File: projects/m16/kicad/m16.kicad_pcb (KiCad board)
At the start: 2 copper layers, 50 x 50 mm, 53 parts, among them P1 ENC1, P2 ENC2, P3 USB_OTG, P4 Molex 475710001, P5 PWR, P7 ESP8266, P8 WS2812, SW1 RST, SW2 HWB, U1 74LS125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

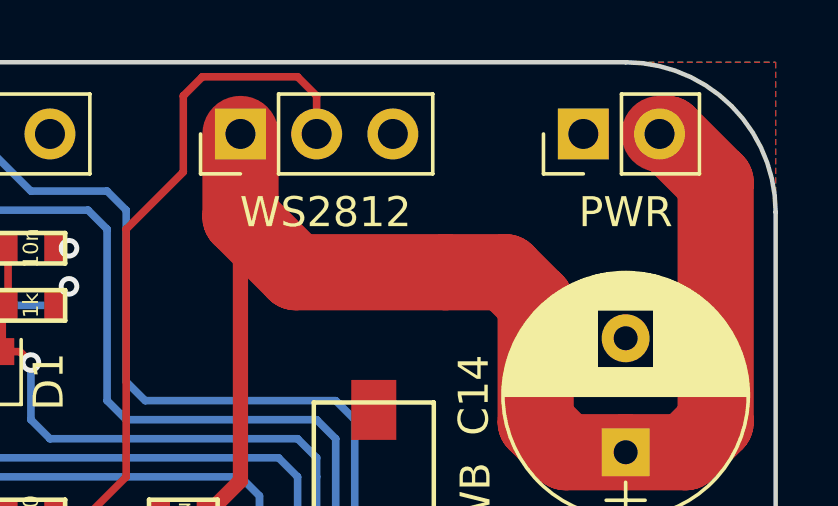
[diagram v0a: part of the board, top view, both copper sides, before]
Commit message: more copper for +5 to ws2812
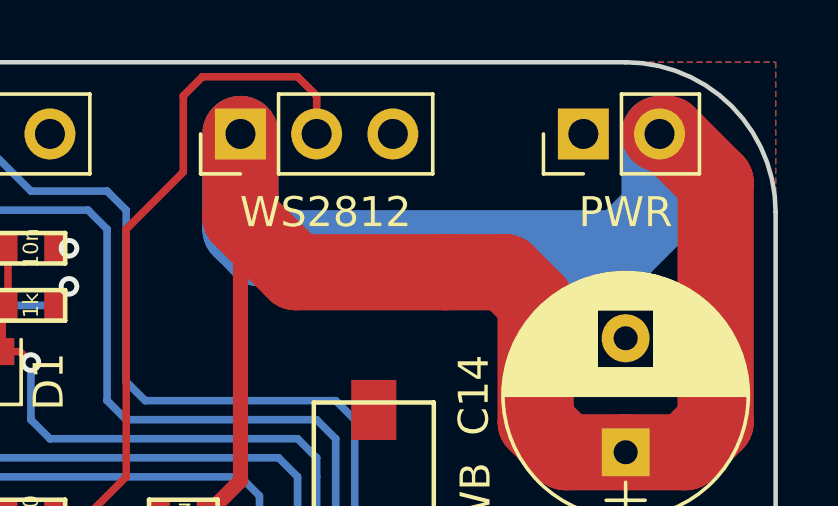
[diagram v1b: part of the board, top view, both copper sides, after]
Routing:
- net +5V: track 183.4 -> 203.9 mm
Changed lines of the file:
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@@
     (thickness 1.6)
     (drawings 14)
-    (tracks 609)
+    (tracks 614)
     (zones 0)
     (modules 53)
@@
     (35 F.Paste user)
     (36 B.SilkS user)
-    (37 F.SilkS user)
+    (37 F.SilkS user hide)
     (38 B.Mask user)
     (39 F.Mask user)
@@
   )
   (setup
-    (last_trace_width 0.254)
+    (last_trace_width 2.54)
     (user_trace_width 0.254)
     (user_trace_width 0.508)
@@
     (mod_text_size 1 1)
     (mod_text_width 0.15)
-    (pad_size 1.7 1.7)
-    (pad_drill 1)
+    (pad_size 1.6 1.6)
+    (pad_drill 0.8)
     (pad_to_mask_clearance 0.2)
     (aux_axis_origin 0 0)
@@
       (net 3 +5V) (zone_connect 2))
     (pad 2 thru_hole circle (at 3.8 0 90) (size 1.6 1.6) (drill 0.8) (layers *.Cu *.Mask)
-      (net 1 GND))
+      (net 1 GND) (zone_connect 2))
     (model ${KISYS3DMOD}/Capacitors_THT.3dshapes/CP_Radial_D8.0mm_P3.80mm.wrl
       (at (xyz 0 0 0))
@@
   (segment (start 143.05 108.95) (end 144 108) (width 0.508) (layer F.Cu) (net 2))
   (segment (start 143 113.95) (end 143.05 114) (width 0.508) (layer F.Cu) (net 2))
+  (segment (start 151.13 72.39) (end 151.13 74.93) (width 2.54) (layer B.Cu) (net 3))
+  (segment (start 137.16 75.565) (end 137.16 72.39) (width 2.54) (layer B.Cu) (net 3))
+  (segment (start 137.795 76.2) (end 137.16 75.565) (width 2.54) (layer B.Cu) (net 3))
+  (segment (start 149.86 76.2) (end 137.795 76.2) (width 2.54) (layer B.Cu) (net 3))
+  (segment (start 151.13 74.93) (end 149.86 76.2) (width 2.54) (layer B.Cu) (net 3))
   (segment (start 124.46 102.997) (end 123.063 102.997) (width 0.508) (layer F.Cu) (net 3))
   (segment (start 122.428 103.632) (end 122.428 104.775) (width 0.508) (layer F.Cu) (net 3))
@@
   (segment (start 135.715 85.2) (end 135.715 85.5) (width 0.508) (layer F.Cu) (net 3))
   (segment (start 150 83) (end 148 83) (width 2.54) (layer F.Cu) (net 3))
+  (segment (start 148 83) (end 147 82) (width 2.54) (layer F.Cu) (net 3))
+  (segment (start 147 82) (end 147 78) (width 2.54) (layer F.Cu) (net 3))
+  (segment (start 147 78) (end 146 77) (width 2.54) (layer F.Cu) (net 3))
+  (segment (start 146 77) (end 144 77) (width 2.54) (layer F.Cu) (net 3))
+  (segment (start 137.16 75.16) (end 137.16 72.39) (width 2.54) (layer F.Cu) (net 3))
+  (segment (start 139 77) (end 144 77) (width 2.54) (layer F.Cu) (net 3))
   (segment (start 137.16 75.16) (end 139 77) (width 2.54) (layer F.Cu) (net 3))
-  (segment (start 139 77) (end 144 77) (width 2.54) (layer F.Cu) (net 3))
-  (segment (start 137.16 75.16) (end 137.16 72.39) (width 2.54) (layer F.Cu) (net 3))
-  (segment (start 146 77) (end 144 77) (width 2.54) (layer F.Cu) (net 3))
-  (segment (start 147 78) (end 146 77) (width 2.54) (layer F.Cu) (net 3))
-  (segment (start 147 82) (end 147 78) (width 2.54) (layer F.Cu) (net 3))
-  (segment (start 148 83) (end 147 82) (width 2.54) (layer F.Cu) (net 3))
   (segment (start 151.13 72.39) (end 151.39 72.39) (width 2.54) (layer F.Cu) (net 3))
   (segment (start 151.39 72.39) (end 153 74) (width 2.54) (layer F.Cu) (net 3))

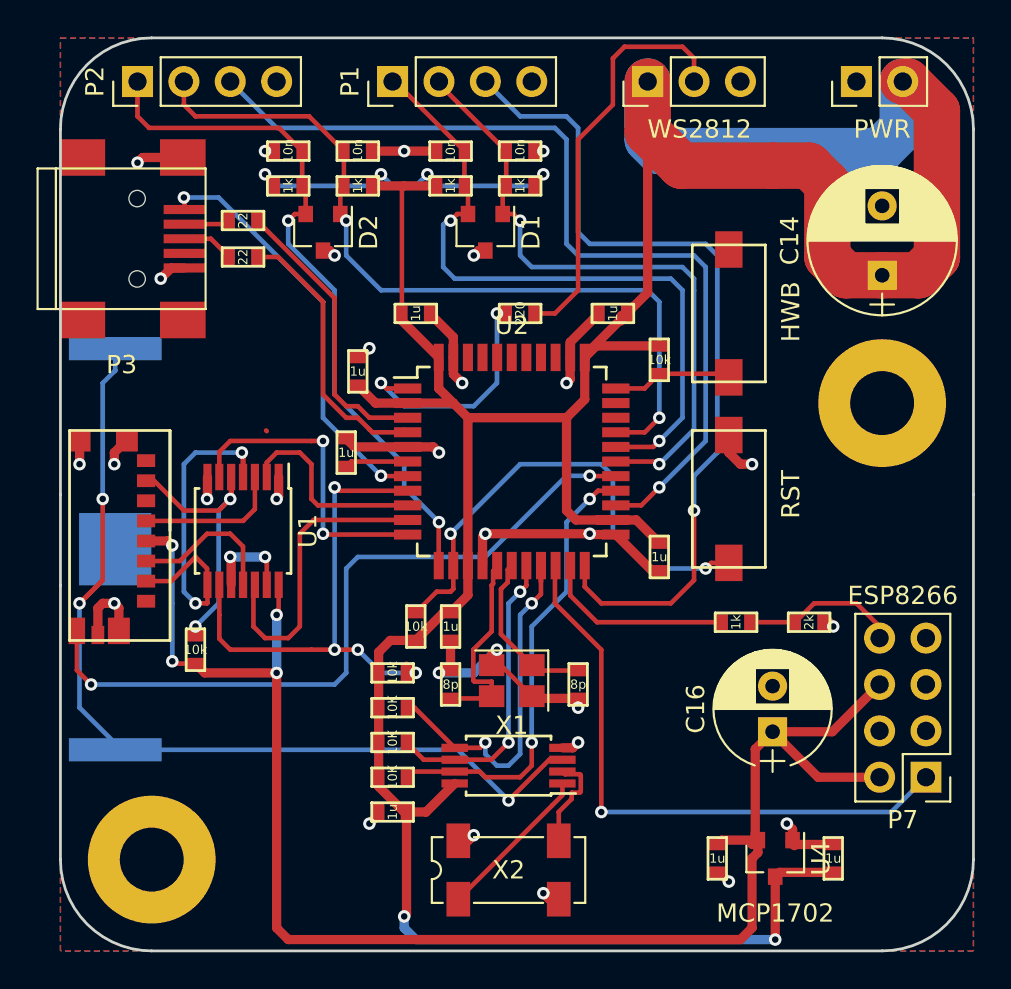
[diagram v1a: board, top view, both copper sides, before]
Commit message: adding IR header; beefing up 3v3 regul
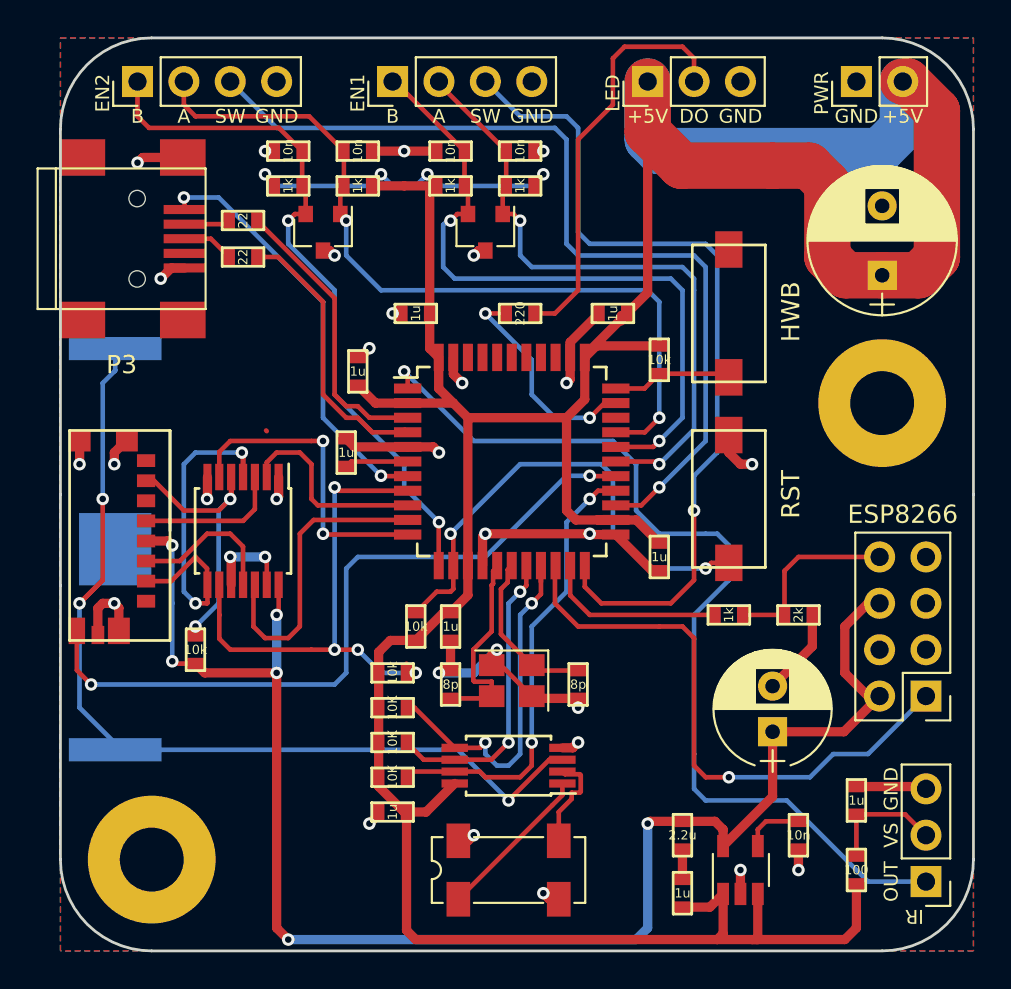
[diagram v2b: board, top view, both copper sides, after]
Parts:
- added C18: 1u, DigitalCave:SM0603_VALUE, F.Cu at (148.6, 111.8)
- added C19: 10n, DigitalCave:SM0603_VALUE, F.Cu at (145.4, 113.7)
- added J1: IR, Pin_Headers:Pin_Header_Straight_1x03_Pitch2.54mm, F.Cu at (152.4, 116.2)
- added R17: 100, DigitalCave:SM0603_VALUE, F.Cu at (148.6, 115.6)
- C17: value 1u -> 2.2u
- U4: value MCP1702 -> MIC5219-3.3BM5; footprint TO_SOT_Packages_SMD:SOT-23 -> TO_SOT_Packages_SMD:TSOT-23-5
- moved C13 8.47 mm to (139.1, 116.8)
- moved P7 4.44 mm to (152.4, 106.0)
- moved C17 2.29 mm to (139.1, 113.7)
- moved U4 2.01 mm to (142.2, 115.6), turned to 90 degrees
- moved R15 0.71 mm to (145.4, 101.6)
- moved R14 0.56 mm to (141.6, 101.6)
- turned C8 to 180 degrees
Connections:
- U2 pad 1: /LED -> /IROUT
- U2 pad 32: Net-(U2-Pad32) -> /LED
- U4 pad 1: GND -> +5V
- U4 pad 2: +3V3 -> GND
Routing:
- net /IROUT: track 0.00 -> 53.2 mm, vias 0 -> 1
- net +5V: track 203.9 -> 211.6 mm, vias 6 -> 4
- net Net-(C18-Pad2): track 0.00 -> 6.57 mm
- net GND: track 76.8 -> 81.8 mm
- net Net-(C19-Pad1): track 0.00 -> 3.32 mm
- net Net-(P7-Pad8): track 8.69 -> 10.2 mm
- net +3V3: track 87.1 -> 86.0 mm, vias 4 -> 6
- net /RX_TX: track 33.1 -> 32.3 mm
- net /LED: track 13.3 -> 12.7 mm
- net /TX_RX: track 10.6 -> 10.0 mm
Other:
- board text added: "+5V"
- board text added: "A"
- board text added: "B"
- board text added: "DO"
- board text added: "EN1"
- board text added: "EN2"
- board text added: "GND"
- board text added: "IR"
- board text added: "LED"
- board text added: "OUT"
- board text added: "PWR"
- board text added: "SW"
- board text added: "VS"

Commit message: adding test point and logo
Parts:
- added J2: TEST_1P, Connectors:PINTST, F.Cu at (144.1, 90.2)
- added WJ20: VAL**, DigitalCave:WJ20, F.Cu at (119.4, 111.8)
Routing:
- net Net-(J2-Pad1): track 0.00 -> 17.7 mm
- net +5V: track 211.6 -> 208.8 mm
- net /E2A: track 44.3 -> 45.2 mm

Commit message: cleaning up traces
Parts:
- moved R5 12.7 mm to (113.0, 90.8), turned to 270 degrees
- moved R6 2.62 mm to (122.6, 102.2), turned to 90 degrees
- moved C7 0.90 mm to (121.3, 93.3)
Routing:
- net /CS: track 20.8 -> 10.2 mm
- net +3V3: track 86.0 -> 94.9 mm
- net /SS: track 28.5 -> 22.3 mm, vias 4 -> 2
- net +5V: track 208.8 -> 214.0 mm
- net /DET: track 40.1 -> 36.7 mm
- net /E2B: track 38.7 -> 41.9 mm
- net /DO: track 16.3 -> 13.1 mm, vias 2 -> 0
- net /VBUS: track 23.0 -> 26.0 mm
- net /MOSI: track 16.7 -> 14.5 mm
- net /CLK: track 7.98 -> 9.84 mm
- net /MISO: track 17.1 -> 18.7 mm
- net GND: track 81.8 -> 81.7 mm, vias 31 -> 32

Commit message: more routing cleanup
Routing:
- net +3V3: track 94.9 -> 90.5 mm
- net +BATT: track 52.0 -> 56.4 mm, vias 3 -> 1
- net /DET: track 36.7 -> 34.9 mm
- net GND: track 81.7 -> 83.0 mm, vias 32 -> 31
